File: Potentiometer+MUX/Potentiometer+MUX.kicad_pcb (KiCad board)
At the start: 2 copper layers, 21 parts, among them J1 Conn_01x04, J2 Conn_01x02, J3 Conn_01x08, J4 Conn_01x16

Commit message: Finished Layout
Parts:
- removed C2, C3, C4, C5, C6, C7, C8, C9: 0.1uF, Capacitor_THT:C_Disc_D5.0mm_W2.5mm_P2.50mm
- added REF**: MountingHole_3.2mm_M3_ISO7380_Pad_TopBottom, MountingHole:MountingHole_3.2mm_M3_ISO7380_Pad_TopBottom, F.Cu at (83.0, 181.0)
- added REF**: MountingHole_3.2mm_M3_ISO7380_Pad_TopBottom, MountingHole:MountingHole_3.2mm_M3_ISO7380_Pad_TopBottom, F.Cu at (154.5, 39.0)
- added REF**: MountingHole_3.2mm_M3_ISO7380_Pad_TopBottom, MountingHole:MountingHole_3.2mm_M3_ISO7380_Pad_TopBottom, F.Cu at (83.0, 22.0)
- added REF**: MountingHole_3.2mm_M3_ISO7380_Pad_TopBottom, MountingHole:MountingHole_3.2mm_M3_ISO7380_Pad_TopBottom, F.Cu at (141.0, 181.0)
- moved RV1 90.0 mm to (126.0, 68.0)
- moved RV4 90.0 mm to (126.0, 158.0)
- moved RV2 30.0 mm to (126.0, 98.0)
- moved RV3 30.0 mm to (126.0, 128.0)
- moved J1 23.8 mm to (149.7, 23.7)
- moved J2 20.8 mm to (149.6, 47.0)
- moved J3 17.0 mm to (112.9, 39.8)
- moved J4 17.0 mm to (85.0, 55.0)
- moved C1 9.92 mm to (117.5, 36.5)
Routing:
- net +3.3V: track 15.6 -> 447.4 mm
- net Net-(J4-Pin_13): track 17.8 -> 113.9 mm
- net Net-(J4-Pin_16): track 111.1 -> 19.2 mm
- net Net-(J1-Pin_1): track 0.00 -> 61.2 mm
- net Net-(J1-Pin_2): track 0.00 -> 55.1 mm
- net Net-(J1-Pin_3): track 0.00 -> 51.5 mm
- net Net-(J1-Pin_4): track 0.00 -> 47.9 mm
- net Net-(J4-Pin_14): track 48.8 -> 82.6 mm
- net Net-(J4-Pin_15): track 79.8 -> 51.5 mm
- net Net-(J4-Pin_9): track 29.6 -> 18.9 mm
- net Net-(J4-Pin_10): track 57.0 -> 50.0 mm
- net Net-(J4-Pin_11): track 88.1 -> 81.0 mm
- net Net-(J4-Pin_12): track 119.1 -> 112.1 mm
- added copper zone on B.Cu, net GND
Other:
- board outline added: 83.5 x 171 mm
- board text added: "3.3V"
- board text added: "4x2 Potentiometer + Multiplexer"
- board text added: "GND"
- board text added: "Knob 1"
- board text added: "Knob 2"
- board text added: "Knob 3"
- board text added: "Knob 4"
- board text added: "Knob 5"
- board text added: "Knob 6"
- board text added: "Knob 7"
- board text added: "Knob 8"
- board text added: "S0"
- board text added: "S1"
- board text added: "S2"
- board text added: "SIG"

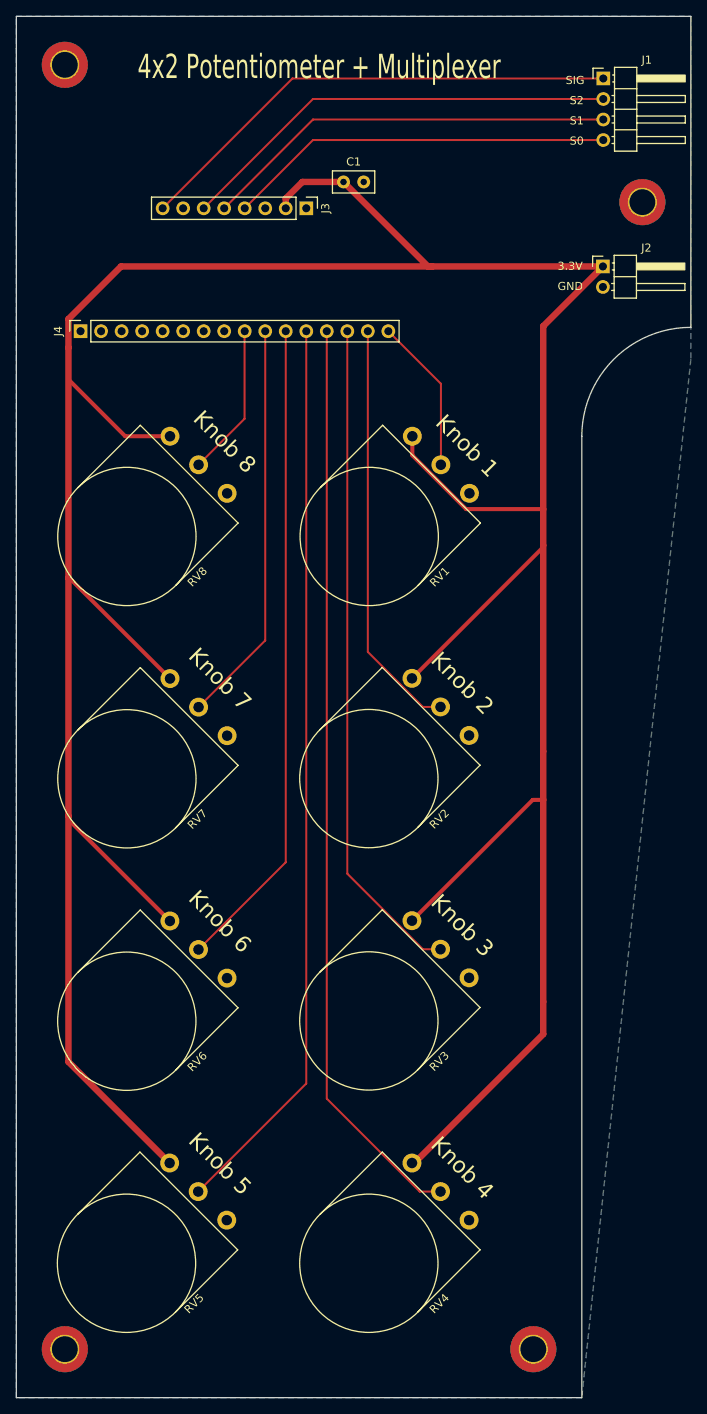
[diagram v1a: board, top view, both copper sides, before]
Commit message: Smaller MUX, Main Board design
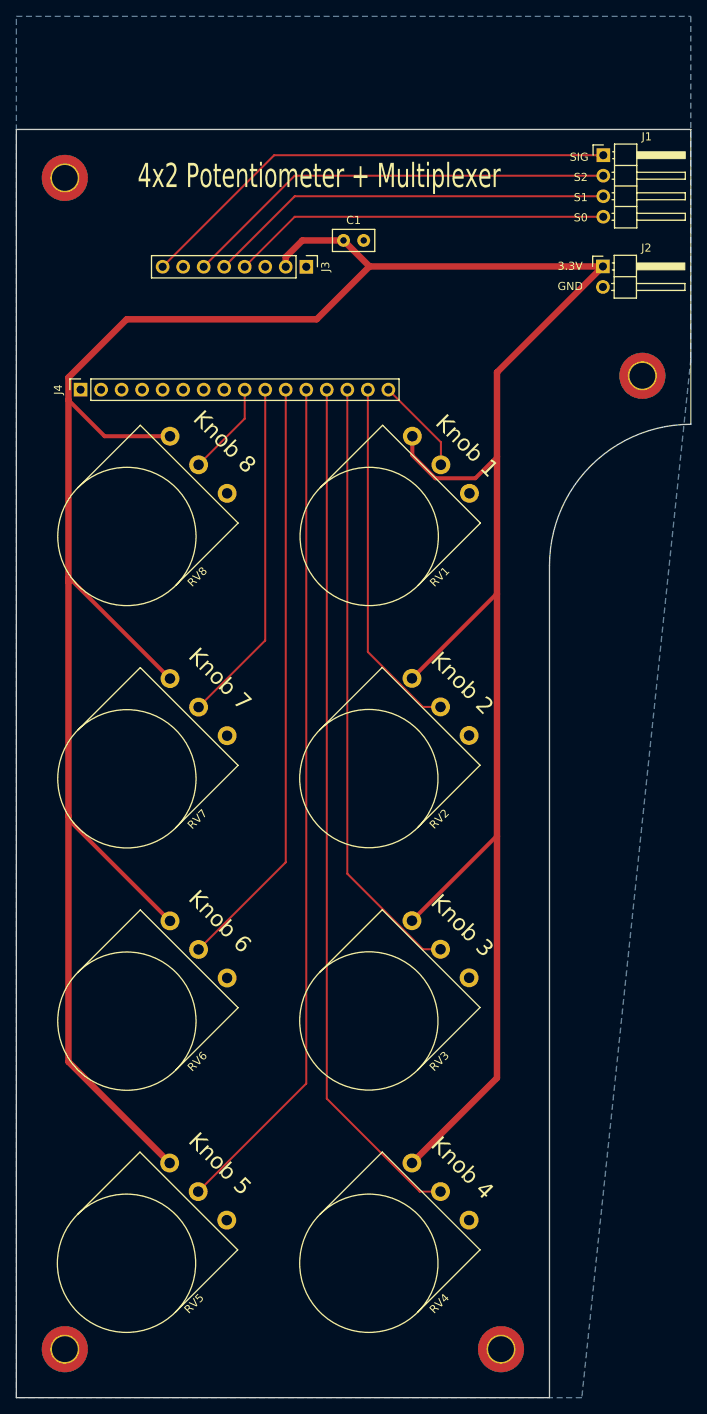
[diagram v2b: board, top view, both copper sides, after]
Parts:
- moved REF** 21.5 mm to (154.5, 60.5)
- moved REF** 14.0 mm to (83.0, 36.0)
- moved J1 9.50 mm to (149.7, 33.2)
- moved C1 7.24 mm to (117.5, 43.7)
- moved J3 7.24 mm to (112.9, 47.0)
- moved J4 7.24 mm to (85.0, 62.2)
- moved REF** 4.00 mm to (137.0, 181.0)
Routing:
- net +3.3V: track 447.4 -> 404.8 mm
- net Net-(J4-Pin_13): track 113.9 -> 106.6 mm
- net Net-(J4-Pin_12): track 112.1 -> 104.8 mm
- net Net-(J4-Pin_11): track 81.0 -> 73.8 mm
- net Net-(J4-Pin_9): track 18.9 -> 11.7 mm
- net Net-(J4-Pin_15): track 51.5 -> 44.3 mm
- net Net-(J4-Pin_10): track 50.0 -> 42.7 mm
- net Net-(J4-Pin_16): track 19.2 -> 12.0 mm
- net Net-(J4-Pin_14): track 82.6 -> 75.3 mm
- net Net-(J1-Pin_4): track 47.9 -> 47.0 mm
- net Net-(J1-Pin_3): track 51.5 -> 50.5 mm
- net Net-(J1-Pin_2): track 55.1 -> 54.1 mm
- net Net-(J1-Pin_1): track 61.2 -> 60.3 mm
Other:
- board size 83.5 x 171 mm -> 83.5 x 157 mm
